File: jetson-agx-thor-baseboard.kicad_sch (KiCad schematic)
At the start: 4 parts

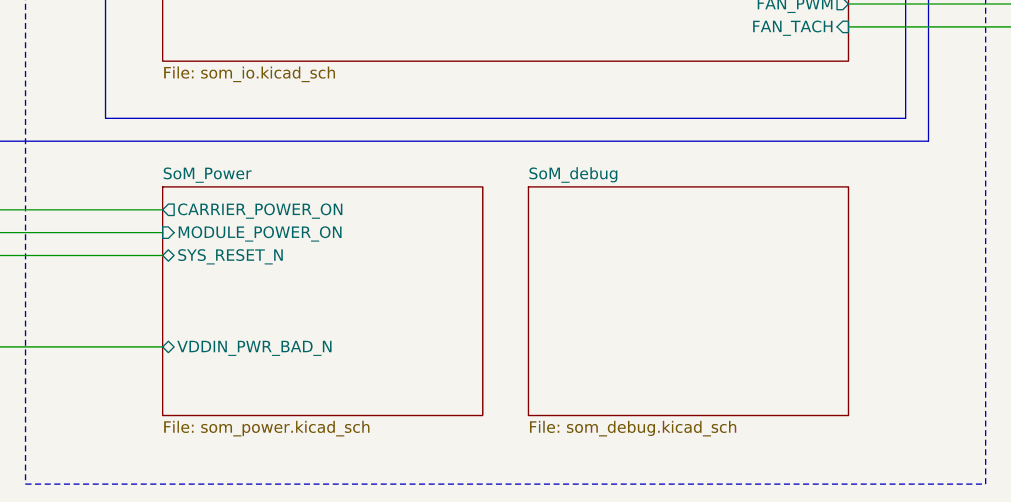
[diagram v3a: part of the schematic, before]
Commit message: [#82837] Add JTAG debug section to SoM_IO sheet. Delete SoM_Debug sheet and rearrange schematic pages
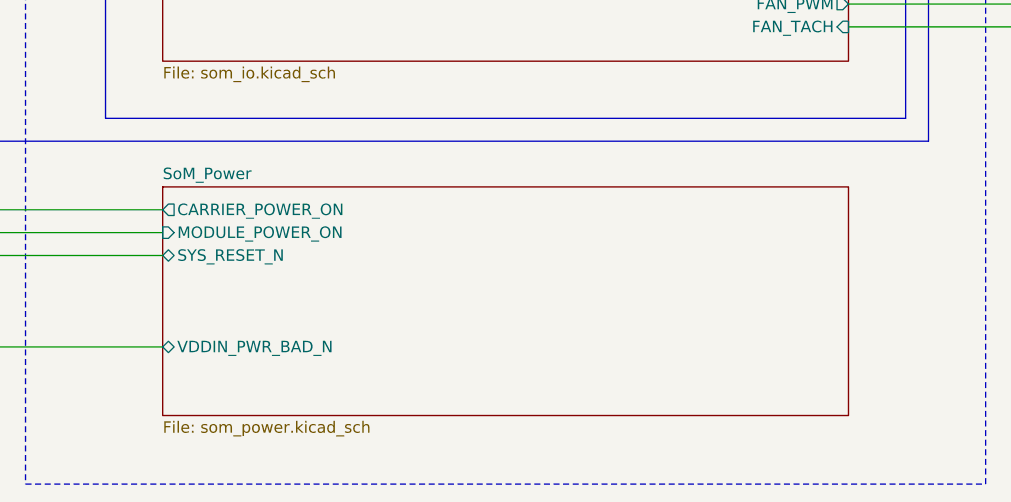
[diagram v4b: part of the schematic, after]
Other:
- removed sheet SoM_debug
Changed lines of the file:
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@@
 			(project "jetson-agx-thor-baseboard"
 				(path "/f569b0be-0afd-48b7-93ee-28582a4c645c"
-					(page "10")
+					(page "9")
 				)
 			)
@@
 			(project "jetson-agx-thor-baseboard"
 				(path "/f569b0be-0afd-48b7-93ee-28582a4c645c"
-					(page "6")
+					(page "5")
 				)
 			)
@@
 	(sheet
 		(at 177.8 228.6)
-		(size 35.56 25.4)
+		(size 76.2 25.4)
 		(exclude_from_sim no)
 		(in_bom yes)
@@
 			(project "jetson-agx-thor-baseboard"
 				(path "/f569b0be-0afd-48b7-93ee-28582a4c645c"
-					(page "7")
+					(page "6")
 				)
 			)
@@
 			(project "jetson-agx-thor-baseboard"
 				(path "/f569b0be-0afd-48b7-93ee-28582a4c645c"
-					(page "13")
+					(page "12")
 				)
 			)
@@
 			(project "jetson-agx-thor-baseboard"
 				(path "/f569b0be-0afd-48b7-93ee-28582a4c645c"
-					(page "11")
-				)
-			)
-		)
-	)
-	(sheet
-		(at 218.44 228.6)
-		(size 35.56 25.4)
-		(exclude_from_sim no)
-		(in_bom yes)
-		(on_board yes)
-		(dnp no)
-		(fields_autoplaced yes)
-		(stroke
-			(width 0.1524)
-			(type solid)
-		)
-		(fill
-			(color 0 0 0 0.0000)
-		)
-		(property "Sheetname" "SoM_debug"
-			(at 218.44 227.8884 0)
-			(effects
-				(font
-					(size 1.27 1.27)
-				)
-				(justify left bottom)
-			)
-		)
-		(property "Sheetfile" "som_debug.kicad_sch"
-			(at 218.44 254.5846 0)
-			(effects
-				(font
-					(size 1.27 1.27)
-				)
-				(justify left top)
-			)
-		)
-		(instances
-			(project "jetson-agx-thor-baseboard"
-				(path "/f569b0be-0afd-48b7-93ee-28582a4c645c"
-					(page "5")
+					(page "10")
 				)
 			)
@@
 			(project "jetson-agx-thor-baseboard"
 				(path "/f569b0be-0afd-48b7-93ee-28582a4c645c"
-					(page "15")
+					(page "14")
 				)
 			)
@@
 			(project "jetson-agx-thor-baseboard"
 				(path "/f569b0be-0afd-48b7-93ee-28582a4c645c"
-					(page "9")
+					(page "8")
 				)
 			)
@@
 			(project "jetson-agx-thor-baseboard"
 				(path "/f569b0be-0afd-48b7-93ee-28582a4c645c"
-					(page "12")
+					(page "11")
 				)
 			)
@@
 			(project "jetson-agx-thor-baseboard"
 				(path "/f569b0be-0afd-48b7-93ee-28582a4c645c"
-					(page "8")
+					(page "7")
 				)
 			)
@@
 			(project "jetson-agx-thor-baseboard"
 				(path "/f569b0be-0afd-48b7-93ee-28582a4c645c"
-					(page "14")
-				)
-			)
+					(page "13")
+				)
+			)

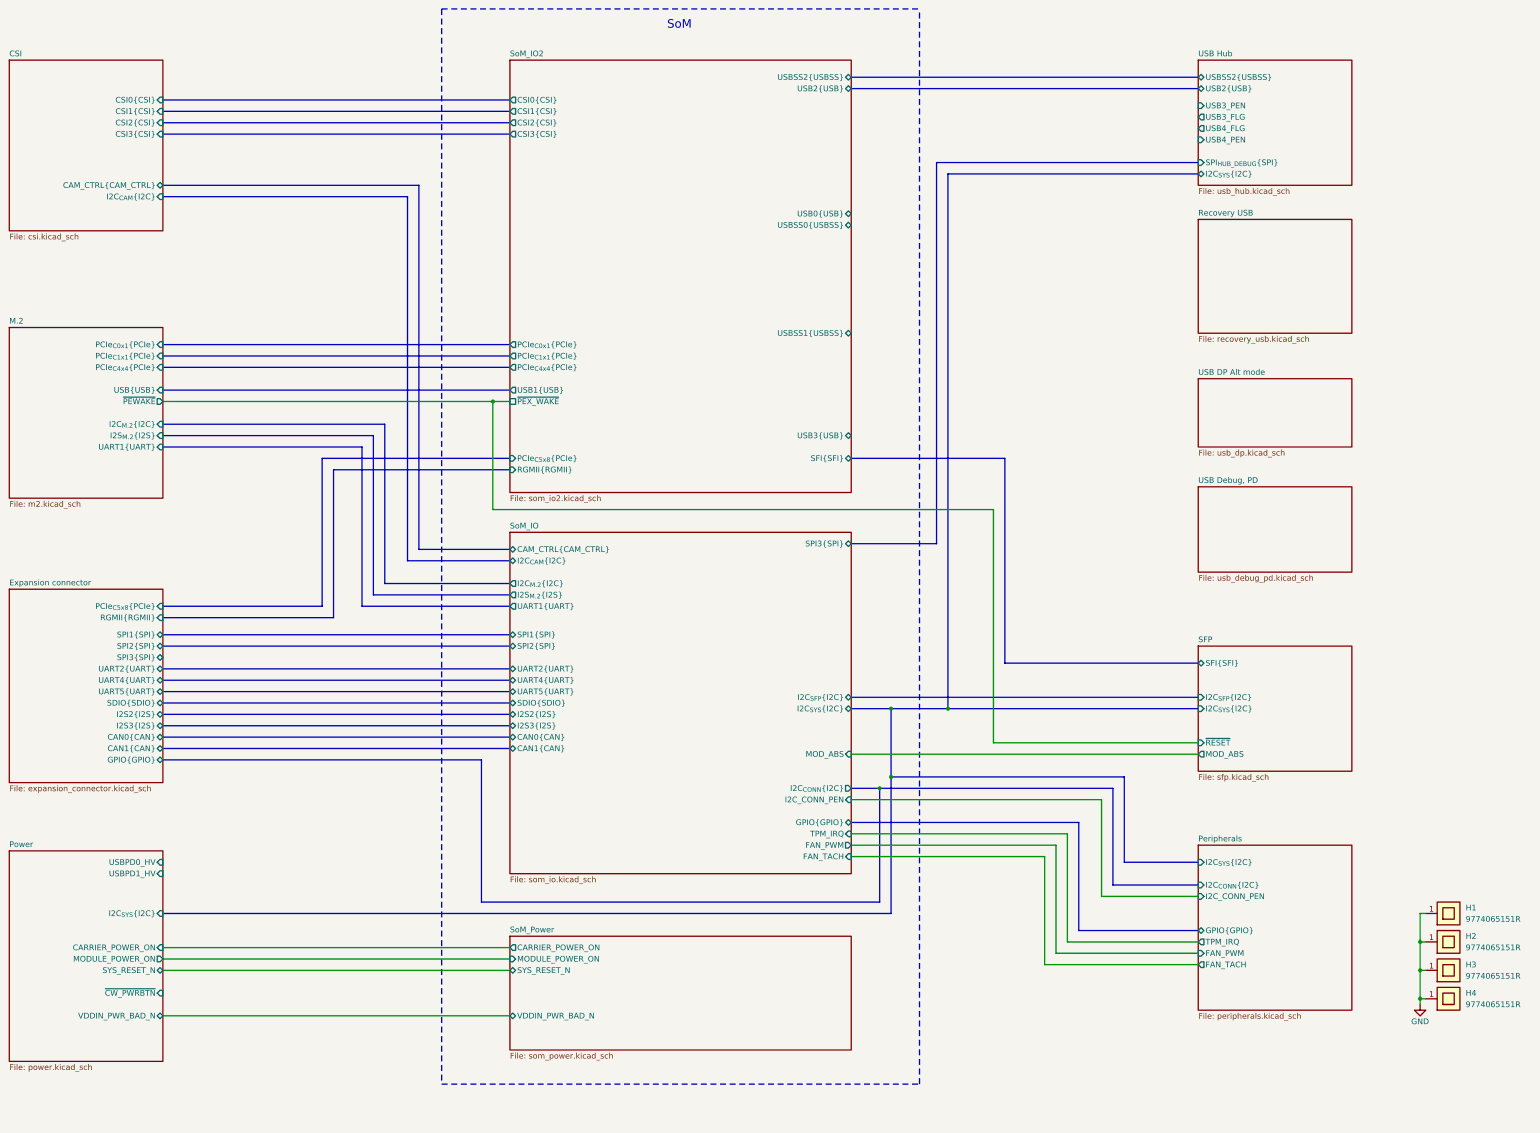
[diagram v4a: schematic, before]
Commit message: [#82837] Wire USB section on root schematic
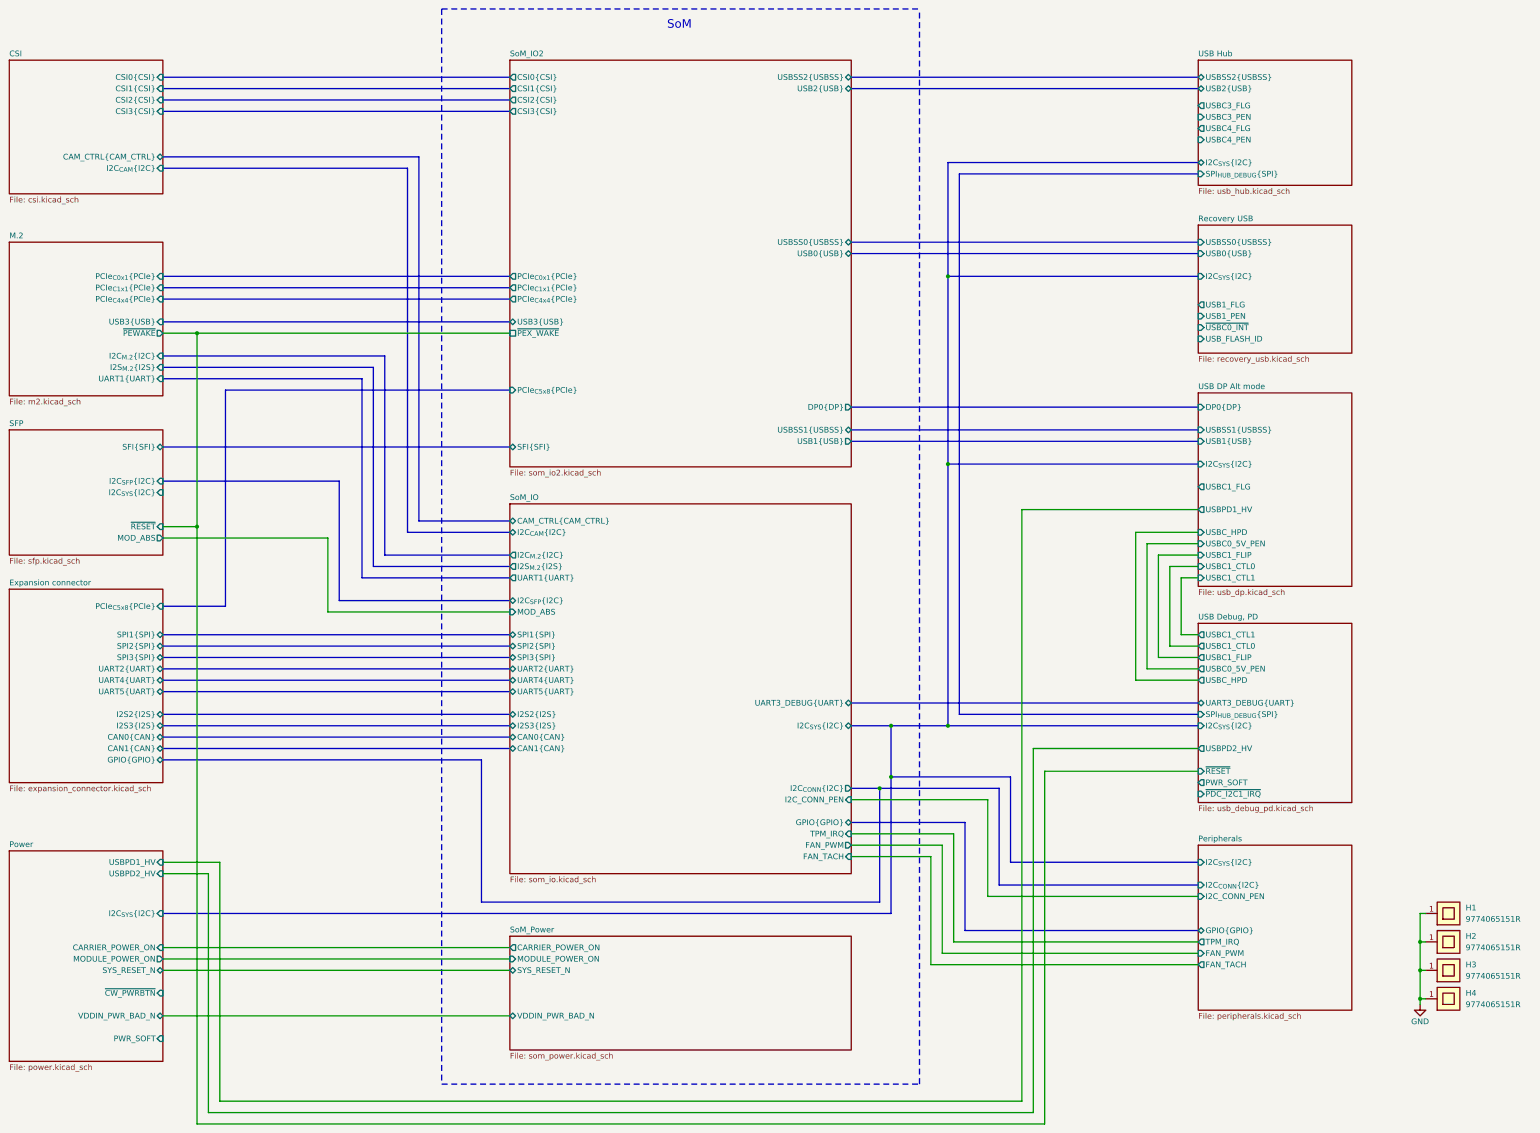
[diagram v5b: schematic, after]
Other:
- sheet Expansion connector ports: added none; removed RGMII{RGMII}, SDIO{SDIO}
- sheet M.2 ports: added USB3{USB}; removed USB{USB}
- sheet Power ports: added PWR_SOFT, USBPD2_HV; removed USBPD0_HV
- sheet Recovery USB ports: added I2C_{SYS}{I2C}, USB0{USB}, USB1_FLG, USB1_PEN, USBSS0{USBSS}, USB_FLASH_ID, ~{USBC0_INT}; removed none
- sheet SoM_IO ports: added UART3_DEBUG{UART}; removed SDIO{SDIO}
- sheet SoM_IO2 ports: added DP0{DP}; removed RGMII{RGMII}
- sheet USB DP Alt mode ports: added DP0{DP}, I2C_{SYS}{I2C}, USB1{USB}, USBC0_5V_PEN, USBC1_CTL0, USBC1_CTL1, USBC1_FLG, USBC1_FLIP, USBC_HPD, USBPD1_HV, USBSS1{USBSS}; removed none
- sheet USB Debug, PD ports: added I2C_{SYS}{I2C}, PWR_SOFT, SPI_{HUB_DEBUG}{SPI}, UART3_DEBUG{UART}, USBC0_5V_PEN, USBC1_CTL0, USBC1_CTL1, USBC1_FLIP, USBC_HPD, USBPD2_HV, ~{PDC_I2C1_IRQ}, ~{RESET}; removed none
- sheet USB Hub ports: added USBC3_FLG, USBC3_PEN, USBC4_FLG, USBC4_PEN; removed USB3_FLG, USB3_PEN, USB4_FLG, USB4_PEN

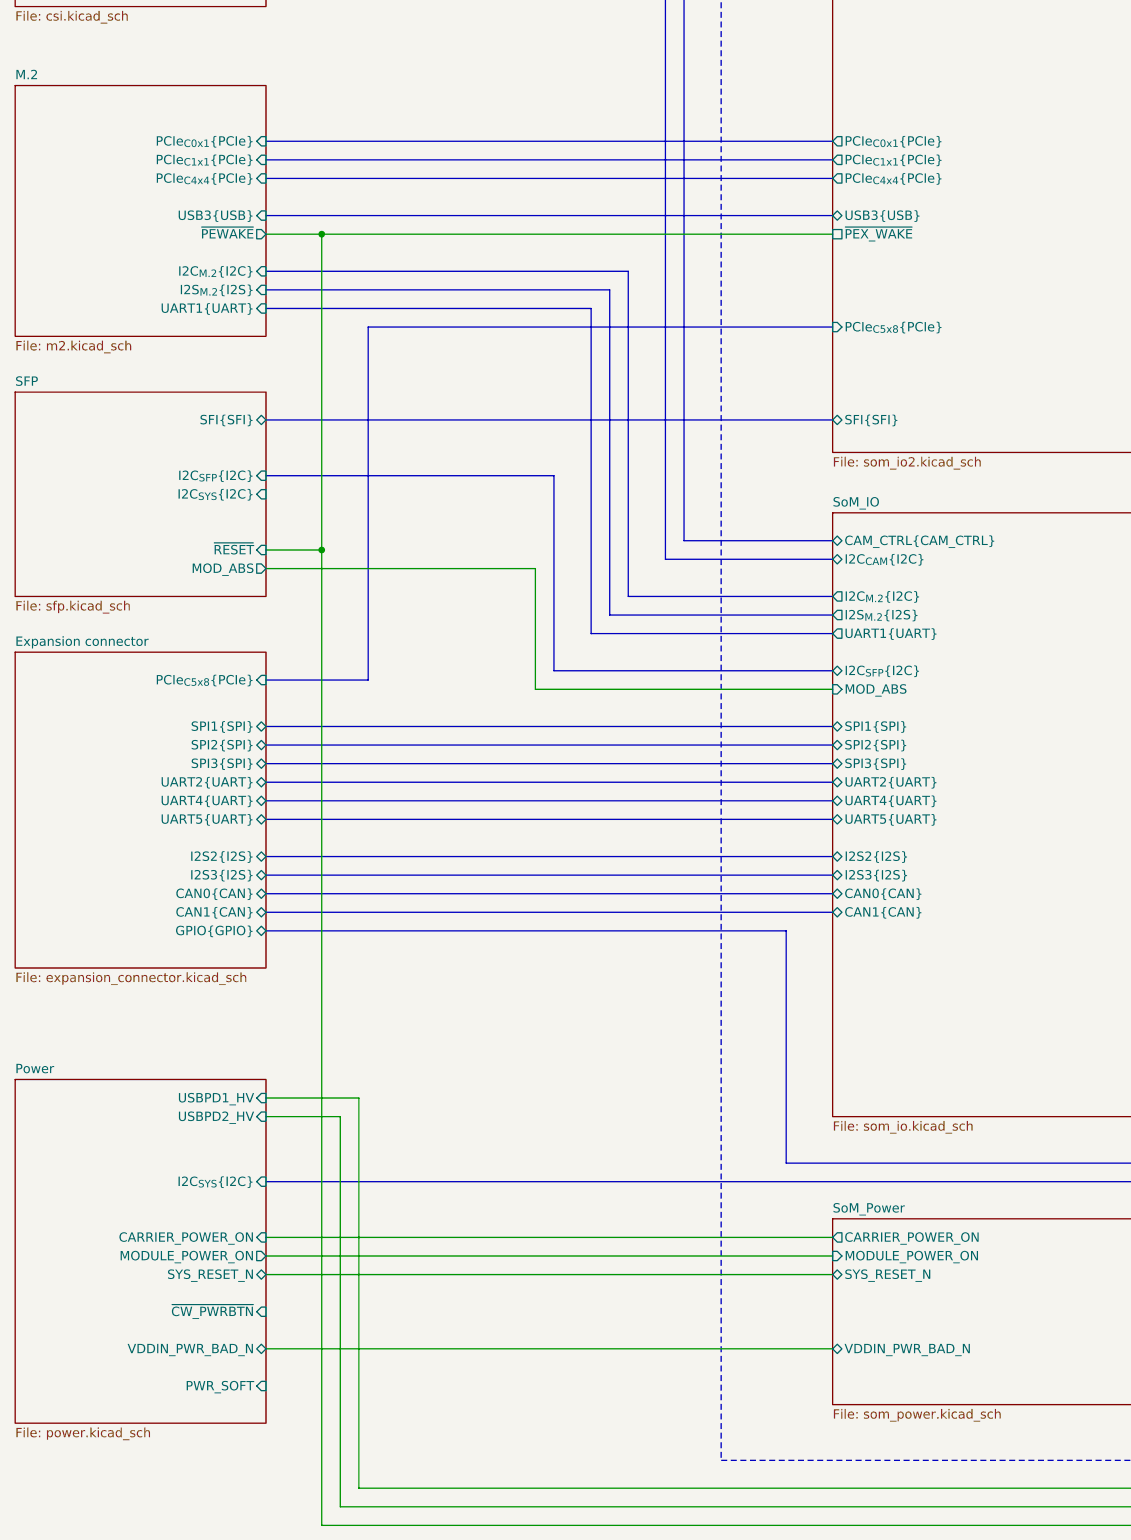
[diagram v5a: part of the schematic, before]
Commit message: [#82837] Map interfaces on expansion connector
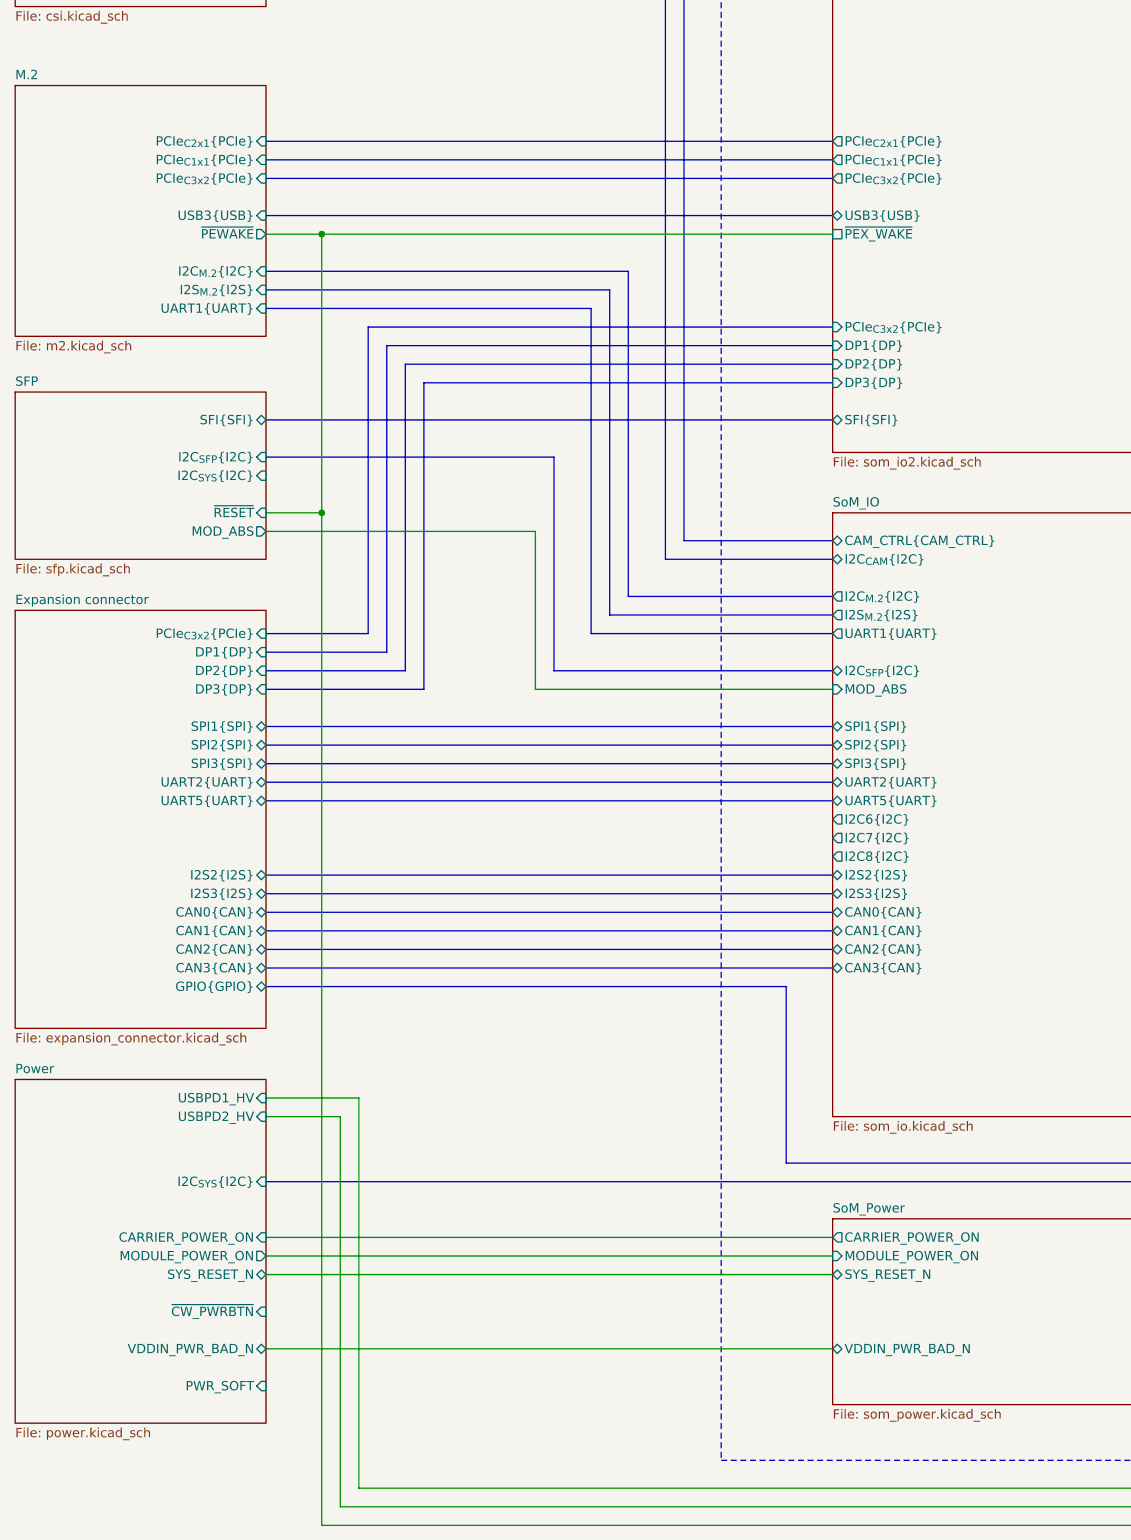
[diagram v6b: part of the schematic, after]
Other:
- sheet Expansion connector ports: added CAN2{CAN}, CAN3{CAN}, DP1{DP}, DP2{DP}, DP3{DP}, PCIe_{C3x2}{PCIe}; removed PCIe_{C5x8}{PCIe}, UART4{UART}
- sheet M.2 ports: added PCIe_{C2x1}{PCIe}, PCIe_{C3x2}{PCIe}; removed PCIe_{C0x1}{PCIe}, PCIe_{C4x4}{PCIe}
- sheet SoM_IO ports: added CAN2{CAN}, CAN3{CAN}, I2C6{I2C}, I2C7{I2C}, I2C8{I2C}; removed UART4{UART}
- sheet SoM_IO2 ports: added DP1{DP}, DP2{DP}, DP3{DP}, PCIe_{C2x1}{PCIe}, PCIe_{C3x2}{PCIe}; removed PCIe_{C0x1}{PCIe}, PCIe_{C4x4}{PCIe}, PCIe_{C5x8}{PCIe}
